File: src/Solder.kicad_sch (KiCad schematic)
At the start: 7 parts, among them SW1 SW_Push

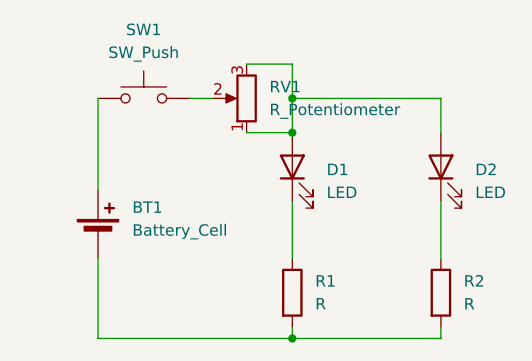
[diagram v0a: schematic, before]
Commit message: Fix potentiometer wiring
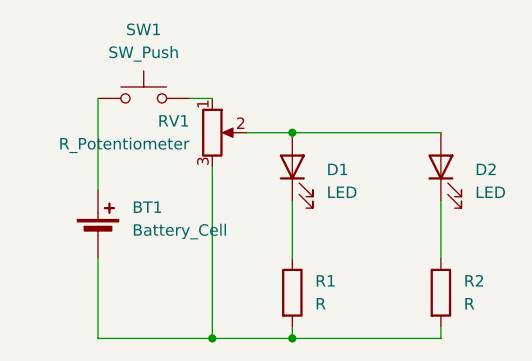
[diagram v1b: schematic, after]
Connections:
- net at D1.2 (A), D2.2 (A): now also RV1.2; no longer RV1.1, RV1.3
- net at SW1.2: now also RV1.1; no longer RV1.2
- net at BT1.2 (-), R1.2, R2.2: now also RV1.3
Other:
- moved on the sheet: RV1
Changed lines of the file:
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@@
 	)
 	(junction
-		(at 127 63.5)
+		(at 118.11 90.17)
 		(diameter 0)
 		(color 0 0 0 0)
@@
 	(wire
 		(pts
-			(xy 115.57 63.5) (xy 118.11 63.5)
+			(xy 118.11 90.17) (xy 105.41 90.17)
 		)
 		(stroke
@@
 	(wire
 		(pts
-			(xy 121.92 67.31) (xy 127 67.31)
-		)
-		(stroke
-			(width 0)
-			(type default)
-		)
-	)
-	(wire
-		(pts
-			(xy 127 90.17) (xy 105.41 90.17)
+			(xy 127 90.17) (xy 118.11 90.17)
 		)
 		(stroke
@@
 	(wire
 		(pts
-			(xy 143.51 63.5) (xy 143.51 67.31)
-		)
-		(stroke
-			(width 0)
-			(type default)
-		)
-	)
-	(wire
-		(pts
-			(xy 127 59.69) (xy 127 63.5)
-		)
-		(stroke
-			(width 0)
-			(type default)
-		)
-	)
-	(wire
-		(pts
-			(xy 121.92 59.69) (xy 127 59.69)
+			(xy 118.11 63.5) (xy 115.57 63.5)
 		)
 		(stroke
@@
 	(wire
 		(pts
-			(xy 127 63.5) (xy 143.51 63.5)
+			(xy 127 67.31) (xy 143.51 67.31)
 		)
 		(stroke
@@
 		(pts
 			(xy 105.41 81.28) (xy 105.41 90.17)
+		)
+		(stroke
+			(width 0)
+			(type default)
+		)
+	)
+	(wire
+		(pts
+			(xy 121.92 67.31) (xy 127 67.31)
 		)
 		(stroke
@@
 	(wire
 		(pts
-			(xy 127 63.5) (xy 127 67.31)
+			(xy 118.11 71.12) (xy 118.11 90.17)
 		)
 		(stroke
@@
 	(symbol
 		(lib_id "Device:R_Potentiometer")
-		(at 121.92 63.5 180)
+		(at 118.11 67.31 0)
 		(unit 1)
 		(exclude_from_sim no)
@@
 		(fields_autoplaced yes)
 		(property "Reference" "RV1"
-			(at 124.46 62.2299 0)
+			(at 115.57 66.0399 0)
 			(effects
 				(font
@@
 		)
 		(property "Value" "R_Potentiometer"
-			(at 124.46 64.7699 0)
+			(at 115.57 68.5799 0)
 			(effects
 				(font
@@
 		)
 		(property "Footprint" "Potentiometer_THT:Potentiometer_Vishay_T73YP_Vertical"
-			(at 121.92 63.5 0)
+			(at 118.11 67.31 0)
 			(effects
 				(font
@@
 		)
 		(property "Datasheet" "~"
-			(at 121.92 63.5 0)
+			(at 118.11 67.31 0)
 			(effects
 				(font
@@
 		)
 		(property "Description" "Potentiometer"
-			(at 121.92 63.5 0)
+			(at 118.11 67.31 0)
 			(effects
 				(font
